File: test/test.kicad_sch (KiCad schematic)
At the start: 14 parts, among them J1 Conn_Coaxial, J2 Conn_Coaxial, U1 OPA188xxD, U2 OPA188xxD

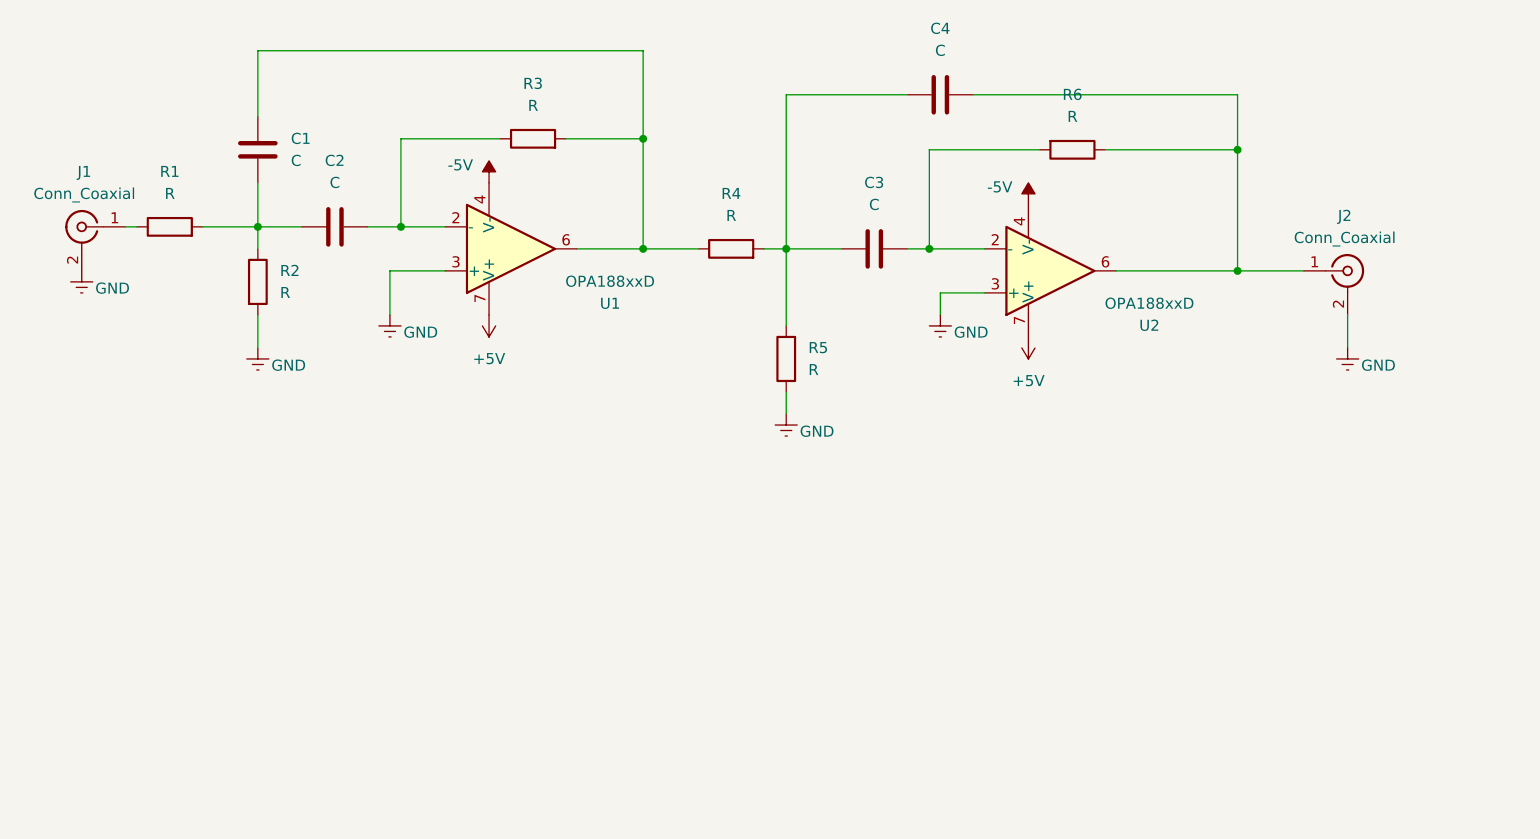
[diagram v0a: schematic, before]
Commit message: Schematic done
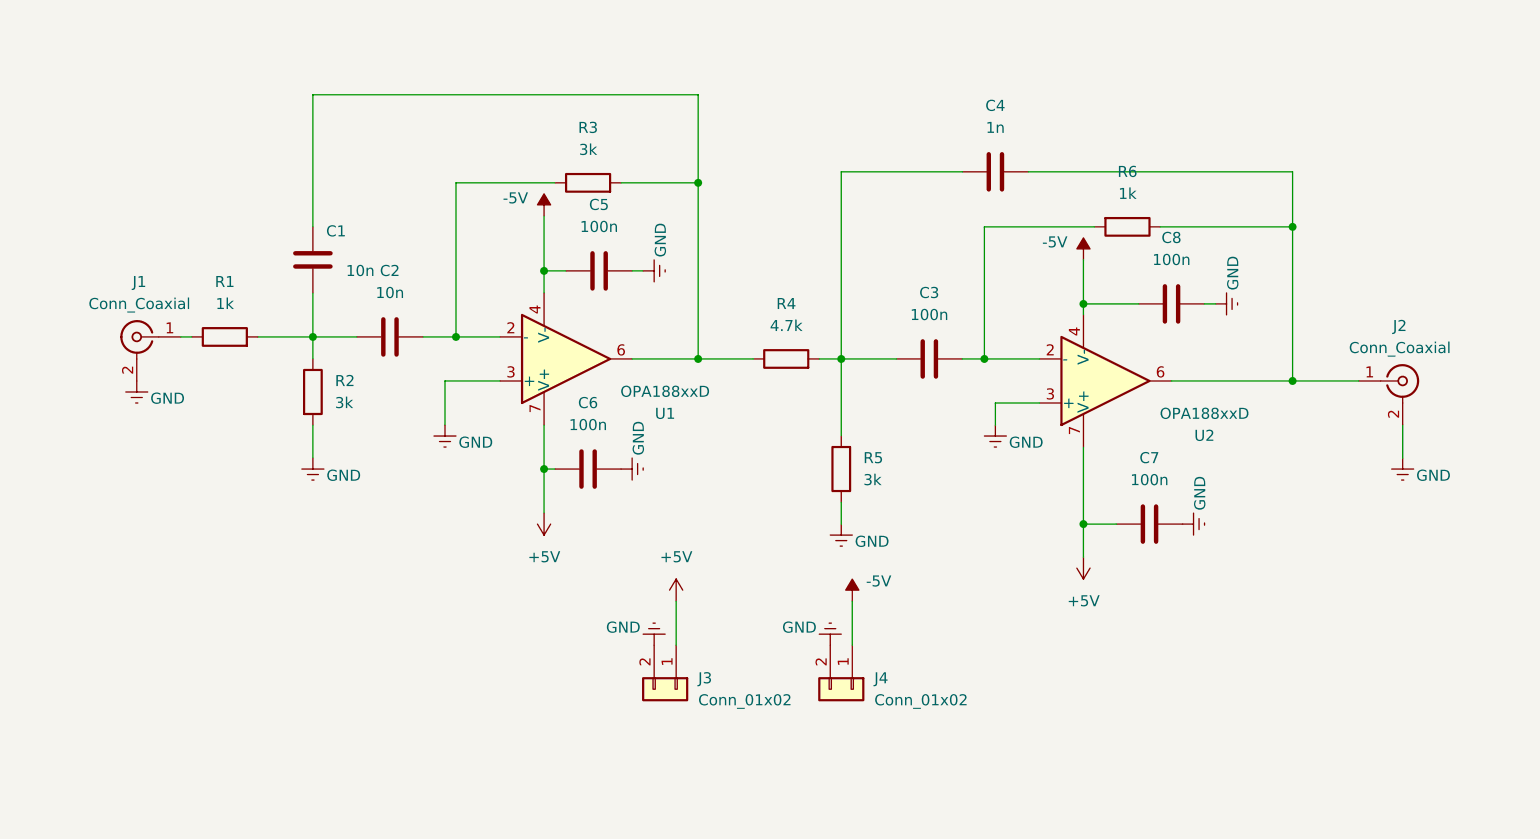
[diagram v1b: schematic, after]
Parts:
- added C5, C6, C7, C8: 100n, Capacitor_SMD:C_0603_1608Metric_Pad1.08x0.95mm_HandSolder, symbol Device:C
- added J3, J4: Conn_01x02, Connector_PinHeader_2.54mm:PinHeader_1x02_P2.54mm_Vertical, symbol Connector_Generic:Conn_01x02
- C1, C2: value C -> 10n; footprint (none) -> Capacitor_SMD:C_0603_1608Metric_Pad1.08x0.95mm_HandSolder
- C3: value C -> 100n; footprint (none) -> Capacitor_SMD:C_0603_1608Metric_Pad1.08x0.95mm_HandSolder
- C4: value C -> 1n; footprint (none) -> Capacitor_SMD:C_0603_1608Metric_Pad1.08x0.95mm_HandSolder
- R1, R6: value R -> 1k; footprint (none) -> Resistor_SMD:R_0603_1608Metric_Pad0.98x0.95mm_HandSolder
- R2, R3, R5: value R -> 3k; footprint (none) -> Resistor_SMD:R_0603_1608Metric_Pad0.98x0.95mm_HandSolder
- R4: value R -> 4.7k; footprint (none) -> Resistor_SMD:R_0603_1608Metric_Pad0.98x0.95mm_HandSolder
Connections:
- net +5V: now also C6.1, C7.1, J3.1 (Pin_1)
- net -5V: now also C5.1, C8.1, J4.1 (Pin_1)
- net GND: now also C5.2, C6.2, C7.2, C8.2, J3.2 (Pin_2), J4.2 (Pin_2)
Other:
- moved on the sheet: C1, C2, C3, C4, J1, J2, R1, R2, R3, R4, R5, R6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

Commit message: Я молодец
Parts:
- added J5, J6, J7, J8: Screw_Terminal_01x01, MountingHole:MountingHole_3.2mm_M3_Pad_Via, symbol Connector:Screw_Terminal_01x01
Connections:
- net GND: now also J5.1 (Pin_1), J6.1 (Pin_1), J7.1 (Pin_1), J8.1 (Pin_1)
